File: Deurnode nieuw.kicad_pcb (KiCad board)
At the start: 2 copper layers, 224.8 x 60.3 mm, 45 parts, among them J1 EXT1, J10 Jumper Output, J11 Jumper Rel./Fet, J12 Screw_Terminal_01x03, J13 Jumper 2 External FET Power, J14 Screw_Terminal_01x02, J15 Screw_Terminal_01x02, J16 Conn_01x02, J17 Conn_01x02, J18 BarrelJack_DC5.5F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

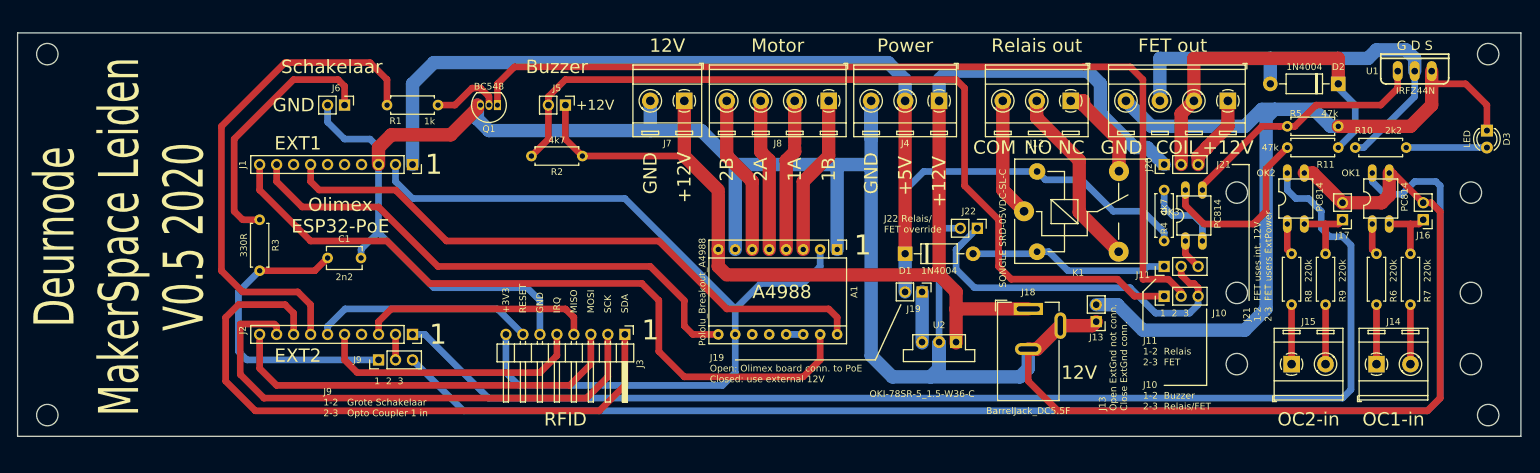
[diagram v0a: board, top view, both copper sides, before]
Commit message: started on re-routing PCB increasing clearance from mains and using netclasses
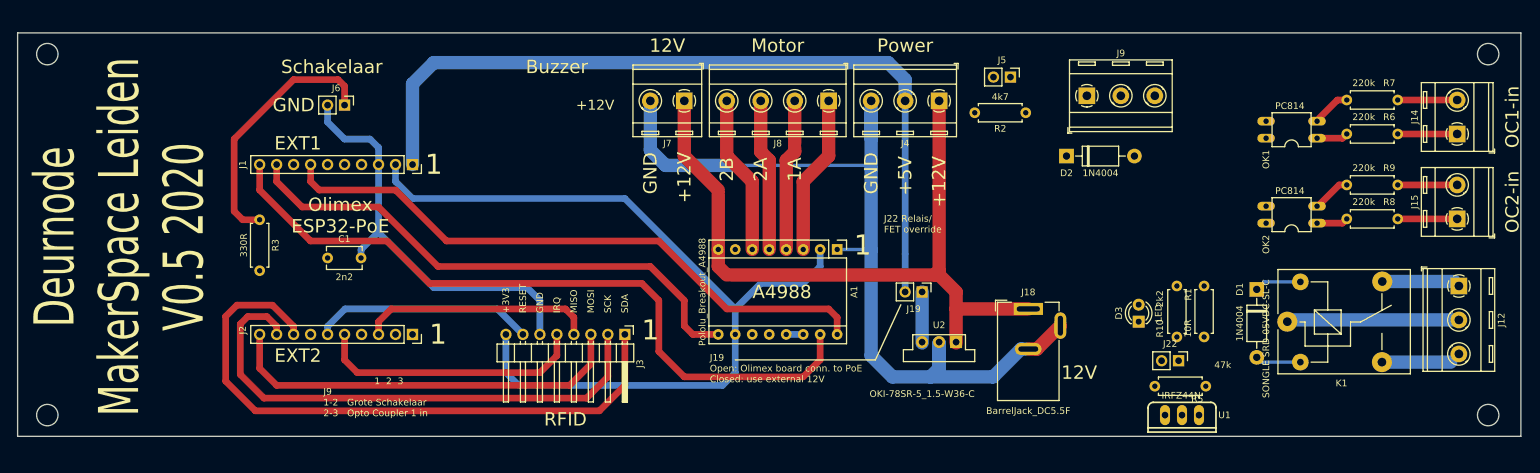
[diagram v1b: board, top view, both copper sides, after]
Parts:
- removed J10: Jumper Output, Connector_PinHeader_2.54mm:PinHeader_1x03_P2.54mm_Vertical
- removed J11: Jumper Rel./Fet, Connector_PinHeader_2.54mm:PinHeader_1x03_P2.54mm_Vertical
- removed J13: Jumper 2 External FET Power, Connector_PinHeader_2.54mm:PinHeader_1x02_P2.54mm_Vertical
- removed J16, J17: Conn_01x02, Connector_PinHeader_2.54mm:PinHeader_1x02_P2.54mm_Vertical
- removed J20: Jumper 1 External FET Power, Connector_PinHeader_2.54mm:PinHeader_1x03_P2.54mm_Vertical
- removed J21: Screw_Terminal_01x04, TerminalBlock_RND:TerminalBlock_RND_205-00289_1x04_P5.08mm_Horizontal
- removed OK3: PC814, PC814:DIL04
- removed Q1: BC548, Package_TO_SOT_THT:TO-92_Inline
- removed R11: 47k, Resistor_THT:R_Axial_DIN0207_L6.3mm_D2.5mm_P7.62mm_Horizontal
- removed R4: 4k7, Resistor_THT:R_Axial_DIN0207_L6.3mm_D2.5mm_P7.62mm_Horizontal
- J22: value Jumper Rel./FET Override -> Force output ON
- J9: value Jumper Input -> Screw_Terminal_01x03; footprint Connector_PinHeader_2.54mm:PinHeader_1x03_P2.54mm_Vertical -> TerminalBlock_RND:TerminalBlock_RND_205-00288_1x03_P5.08mm_Horizontal
- R1: value 1k -> 10R
- moved R1 119.7 mm to (214.9, 116.6), turned to 90 degrees
- moved J9 113.0 mm to (197.4, 80.5), turned to 0 degrees
- moved J5 66.7 mm to (185.9, 77.7)
- moved R2 66.6 mm to (188.2, 83.1)
- moved J12 64.3 mm to (253.0, 109.0), turned to 270 degrees
- moved U1 62.1 mm to (211.6, 128.3), turned to 180 degrees
- moved D3 59.4 mm to (205.1, 114.3), turned to 90 degrees
- moved D1 52.8 mm to (222.8, 109.5), turned to 270 degrees
- moved K1 42.7 mm to (227.3, 114.3)
- moved D2 42.0 mm to (194.3, 89.5), turned to 0 degrees
- moved R5 40.7 mm to (215.1, 124.0), turned to 180 degrees
- moved R10 38.9 mm to (210.8, 116.6), turned to 90 degrees
- moved J14 36.5 mm to (252.7, 86.2), turned to 90 degrees
- moved J22 36.0 mm to (211.1, 120.1)
- moved J15 32.9 mm to (252.7, 98.9), turned to 90 degrees
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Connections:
- A1 pad 13: Net-(A1-Pad13) -> 3V3
- A1 pad 14: Net-(A1-Pad13) -> 3V3
- C1 pad 1: Net-(C1-Pad1) -> GPI36_U1RXD
- D2 pad 1: Net-(D2-Pad1) -> +12V
- D2 pad 2: Net-(D2-Pad2) -> Net-(D1-Pad2)
- D3 pad 1: Net-(D3-Pad1) -> GND
- J22 pad 1: Net-(J10-Pad3) -> Net-(D1-Pad2)
- J5 pad 1: +12V -> Net-(D1-Pad2)
- J5 pad 2: Net-(J10-Pad1) -> +5V
- J9 pad 1: Net-(C1-Pad1) -> +12V
- J9 pad 2: GPI36_U1RXD -> Net-(D1-Pad2)
- J9 pad 3: Net-(J9-Pad3) -> GND
- K1 pad 1: Net-(J12-Pad3) -> Net-(J12-Pad2)
- K1 pad 3: Net-(J12-Pad2) -> Net-(J12-Pad3)
- OK1 pad 4: Net-(J9-Pad3) -> GPI36_U1RXD
- R1 pad 1: Net-(Q1-Pad2) -> Net-(R1-Pad1)
- R10 pad 1: Net-(D2-Pad2) -> Net-(D1-Pad2)
- R2 pad 1: +12V -> Net-(D1-Pad2)
- R2 pad 2: Net-(J10-Pad1) -> +5V
- R3 pad 2: Net-(C1-Pad1) -> GPI36_U1RXD
- R5 pad 1: Net-(OK3-Pad3) -> Net-(R1-Pad1)
- R5 pad 2: Net-(D3-Pad1) -> GND
- U1 pad 1: Net-(OK3-Pad3) -> Net-(R1-Pad1)
- U1 pad 2: Net-(D2-Pad2) -> Net-(D1-Pad2)
- U1 pad 3: Net-(D3-Pad1) -> GND
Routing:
- net GND: track 415.5 -> 193.0 mm
- net Net-(J9-Pad3): track 202.6 -> 0.00 mm
- net GPI39: track 183.4 -> 0.00 mm
- net Net-(J10-Pad2): track 139.2 -> 0.00 mm
- net Net-(J10-Pad1): track 129.1 -> 0.00 mm
- net Net-(D3-Pad1): track 127.8 -> 0.00 mm
- net GPIO16_I2C-SCL: track 75.0 -> 0.00 mm
- net +12V: track 178.4 -> 108.7 mm
- net Net-(D2-Pad2): track 67.1 -> 0.00 mm
- net Net-(D2-Pad1): track 53.7 -> 0.00 mm
- net Net-(J10-Pad3): track 53.1 -> 0.00 mm
- net +5V: track 174.6 -> 126.8 mm
- net Net-(C1-Pad1): track 45.8 -> 0.00 mm
- net Net-(OK3-Pad3): track 38.4 -> 0.00 mm
- net Net-(OK3-Pad4): track 27.2 -> 0.00 mm
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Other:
- outline, holes or cut-outs redrawn
- net class Default: trace_width 0.25 -> 1
- net class MAINS added: clearance 6, trace_width 2, via_dia 0.8, via_drill 0.4
- net class OldDefault added: clearance 0.2, trace_width 0.25, via_dia 0.8, via_drill 0.4
- net class PWRGND added: clearance 0.2, trace_width 2, via_dia 0.8, via_drill 0.4
- board text removed: "1B"
- board text removed: "COIL"
- board text removed: "COM"
- board text removed: "FET out"
- board text removed: "G D S"
- board text removed: "J10 1-2 Buzzer 2-3 Relais/FET"
- board text removed: "J11 1-2 Relais 2-3 FET"
- board text removed: "J13 Open ExtGnd not conn. Close ExtGnd conn."
- board text removed: "J21 1-2 FET uses int. 12V 2-3 FET users ExtPower"
- board text removed: "NC"
- board text removed: "NO"
- board text removed: "Relais out"

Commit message: add groundplane
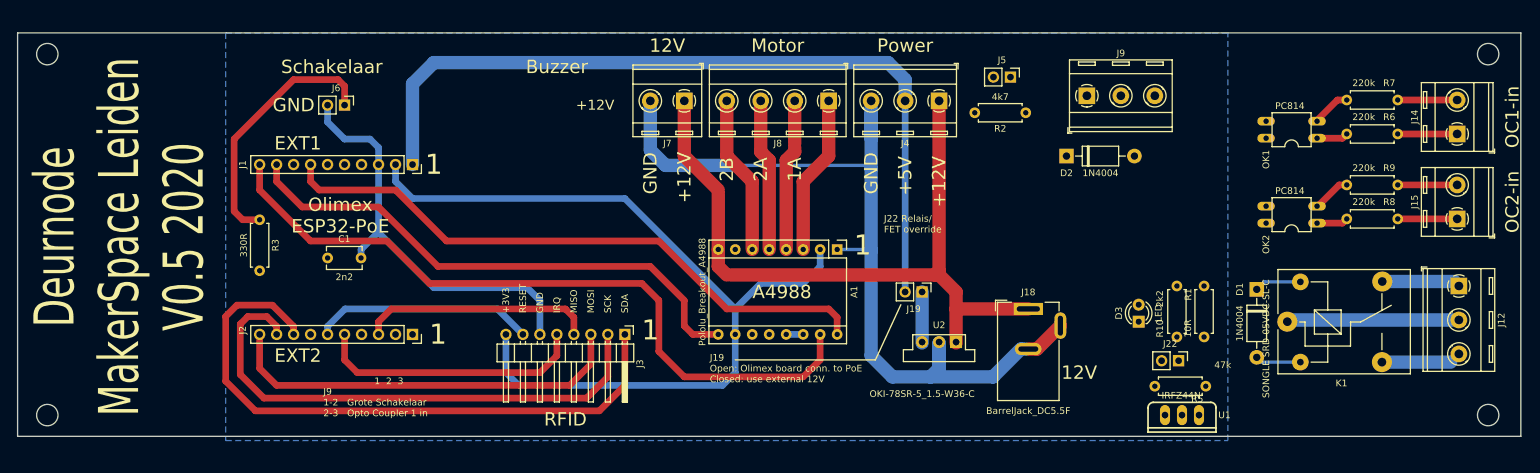
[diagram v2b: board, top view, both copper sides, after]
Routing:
- added copper zone on B.Cu, net GND
